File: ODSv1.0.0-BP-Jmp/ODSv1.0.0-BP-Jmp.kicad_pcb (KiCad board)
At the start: 2 copper layers, 150 x 150 mm, 73 parts, among them J1 Conn_01x16, J10 Conn_02x10_Odd_Even, J11 Conn_02x10_Odd_Even, J12 Conn_02x10_Odd_Even, J13 Conn_02x10_Odd_Even, J14 Conn_02x10_Odd_Even, J15 Conn_02x10_Odd_Even, J16 Conn_02x10_Odd_Even, J17 Conn_02x10_Odd_Even, J18 Conn_02x10_Odd_Even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

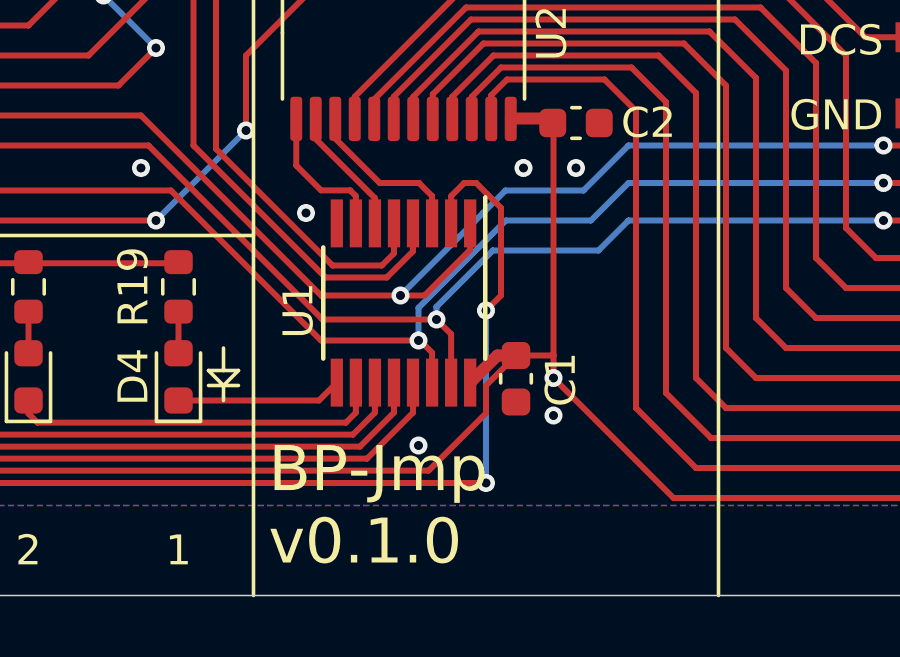
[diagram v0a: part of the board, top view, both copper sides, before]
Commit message: Disconnect BT & BP-Jmp backbone MAX7317 DOUT (#16); make DOUT output pin
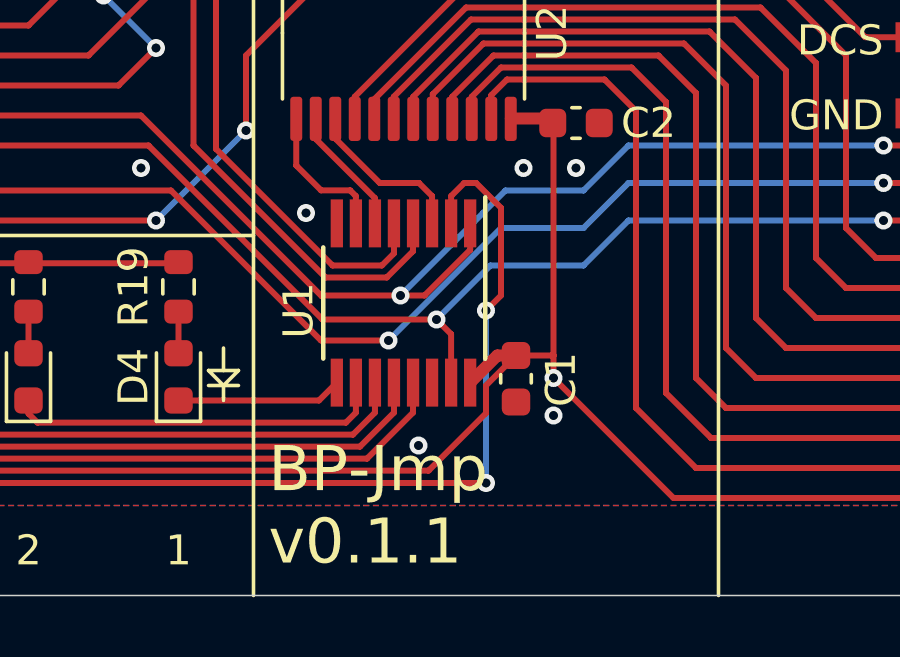
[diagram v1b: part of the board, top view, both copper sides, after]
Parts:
- D1, D2, D3: value Blue -> Green
- D4, D5, D6, D7, D8: value Yellow -> Blue
- R16: value 270 -> 7.5k
- R17: value 1k -> 7.5k
- R18: value 1.2k -> 20k
- R19, R20, R21, R22, R23: value 560 -> 2k
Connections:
- U1 pad 14: /SPI0_CIPO -> (no net)
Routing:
- net /SPI0_CIPO: track 265.8 -> 263.6 mm
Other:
- board text added: "BP-Jmp v0.1.1"
- board text removed: "BP-Jmp v0.1.0"

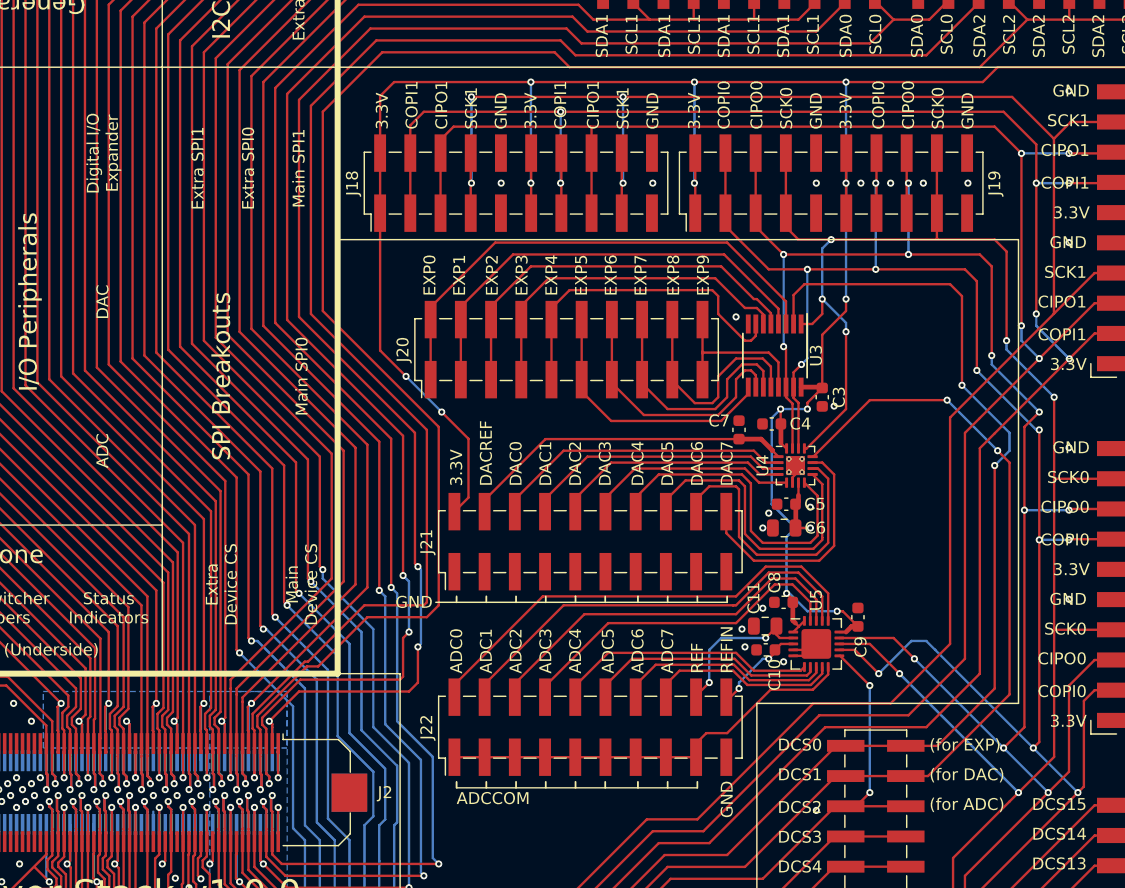
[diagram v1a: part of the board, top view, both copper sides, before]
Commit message: Replace DAC with a second MAX7317 expander with pullup resistors
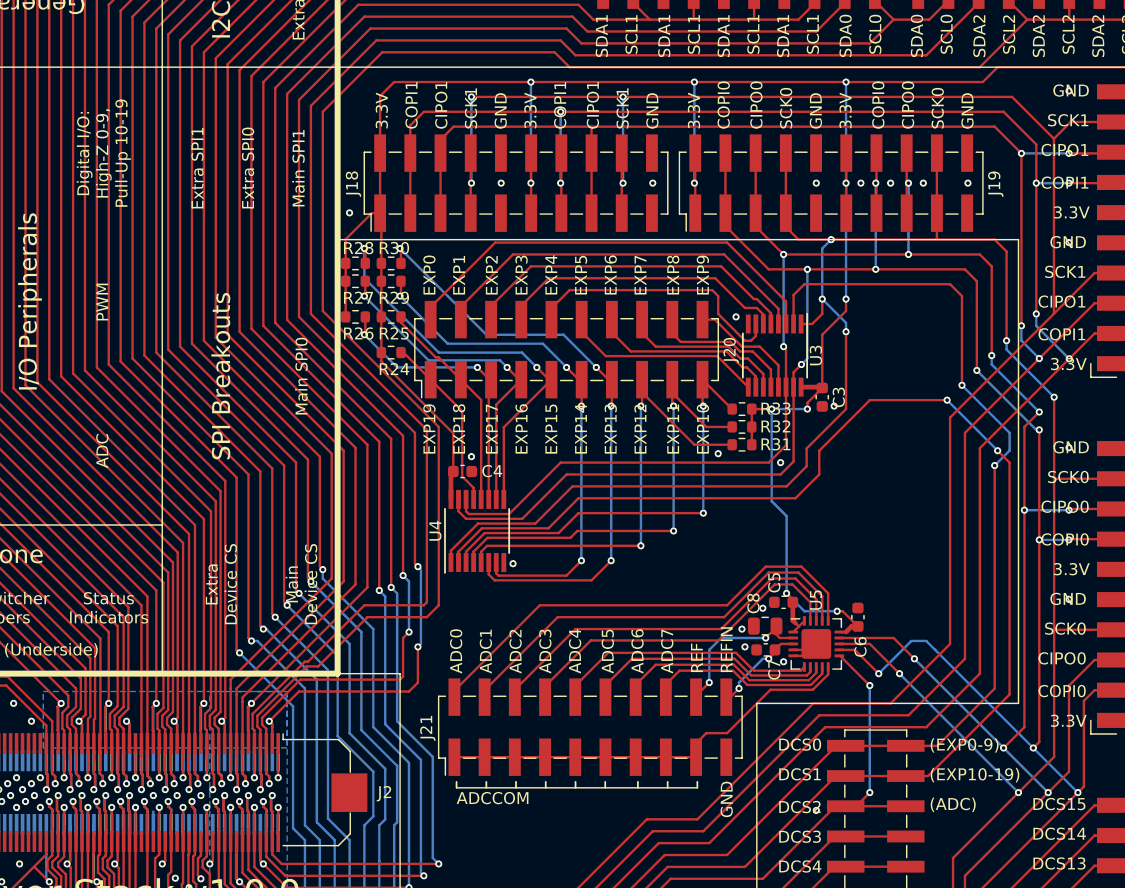
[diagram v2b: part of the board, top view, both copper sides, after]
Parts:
- removed the C5 at (142.5, 150.8)
- removed the C6 at (142.3, 152.8)
- removed the C7 at (138.5, 144.5)
- removed the J21 at (126.0, 153.9)
- added R24: 20k, Resistor_SMD:R_0603_1608Metric, F.Cu at (109.2, 138.0)
- added R25: 20k, Resistor_SMD:R_0603_1608Metric, F.Cu at (109.2, 135.0)
- added R26: 20k, Resistor_SMD:R_0603_1608Metric, F.Cu at (106.2, 135.0)
- added R27: 20k, Resistor_SMD:R_0603_1608Metric, F.Cu at (106.2, 132.0)
- added R28: 20k, Resistor_SMD:R_0603_1608Metric, F.Cu at (106.2, 130.5)
- added R29: 20k, Resistor_SMD:R_0603_1608Metric, F.Cu at (109.2, 132.0)
- added R30: 20k, Resistor_SMD:R_0603_1608Metric, F.Cu at (109.2, 130.5)
- added R31: 20k, Resistor_SMD:R_0603_1608Metric, F.Cu at (138.8, 145.8)
- added R32: 20k, Resistor_SMD:R_0603_1608Metric, F.Cu at (138.8, 144.2)
- added R33: 20k, Resistor_SMD:R_0603_1608Metric, F.Cu at (138.8, 142.8)
- C4: value 0.1uF -> 0.047uF
- U4: value DACx0508xRTE -> MAX7317; footprint Package_DFN_QFN:WQFN-16-1EP_3x3mm_P0.5mm_EP1.6x1.6mm_ThermalVias -> Package_SO:QSOP-16_3.9x4.9mm_P0.635mm
- moved U4 27.3 mm to (116.5, 153.0), turned to 90 degrees
- moved C4 26.3 mm to (115.2, 148.0), turned to 0 degrees
- renumbered C8 to C5, C9 to C6, C10 to C7, C11 to C8, J22 to J21
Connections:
- J20 pad 1: /IO Expander/EXPIO0 -> /IO Expander/EXPIO19
- J20 pad 11: /IO Expander/EXPIO5 -> /IO Expander/EXPIO14
- J20 pad 13: /IO Expander/EXPIO6 -> /IO Expander/EXPIO13
- J20 pad 15: /IO Expander/EXPIO7 -> /IO Expander/EXPIO12
- J20 pad 17: /IO Expander/EXPIO8 -> /IO Expander/EXPIO11
- J20 pad 19: /IO Expander/EXPIO9 -> /IO Expander/EXPIO10
- J20 pad 3: /IO Expander/EXPIO1 -> /IO Expander/EXPIO18
- J20 pad 5: /IO Expander/EXPIO2 -> /IO Expander/EXPIO17
- J20 pad 7: /IO Expander/EXPIO3 -> /IO Expander/EXPIO16
- J20 pad 9: /IO Expander/EXPIO4 -> /IO Expander/EXPIO15
- U4 pad 1: /IO Expander/DACREF -> /SPI0_SCK
- U4 pad 10: /IO Expander/DAC6 -> /IO Expander/EXPIO16
- U4 pad 11: /IO Expander/DAC7 -> /IO Expander/EXPIO17
- U4 pad 12: /~DCS1~ -> /IO Expander/EXPIO18
- U4 pad 13: /SPI0_SCK -> /IO Expander/EXPIO19
- U4 pad 14: /SPI0_COPI -> /SPI0_CIPO
- U4 pad 15: /SPI0_CIPO -> /SPI0_COPI
- U4 pad 2: /IO Expander/DAC0 -> /~DCS1~
- U4 pad 3: /IO Expander/DAC1 -> /IO Expander/EXPIO10
- U4 pad 4: /IO Expander/DAC2 -> /IO Expander/EXPIO11
- U4 pad 5: /IO Expander/DAC3 -> /IO Expander/EXPIO12
- U4 pad 6: GND -> /IO Expander/EXPIO13
- U4 pad 7: +3V3 -> /IO Expander/EXPIO14
- U4 pad 8: /IO Expander/DAC4 -> GND
- U4 pad 9: /IO Expander/DAC5 -> /IO Expander/EXPIO15
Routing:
- net /IO Expander/EXPIO13: track 0.00 -> 51.1 mm, vias 0 -> 4
- net /IO Expander/EXPIO14: track 0.00 -> 43.4 mm, vias 0 -> 4
- net /IO Expander/EXPIO12: track 0.00 -> 39.0 mm, vias 0 -> 2
- net /IO Expander/EXPIO11: track 0.00 -> 38.6 mm, vias 0 -> 2
- net /IO Expander/EXPIO10: track 0.00 -> 37.0 mm, vias 0 -> 2
- net /~DCS1~: track 83.7 -> 118.9 mm
- net /SPI0_SCK: track 253.6 -> 288.8 mm
- net /IO Expander/EXPIO15: track 0.00 -> 34.8 mm, vias 0 -> 2
- net /SPI0_COPI: track 265.3 -> 297.7 mm
- net /SPI0_CIPO: track 263.6 -> 293.5 mm
- net /IO Expander/DACREF: track 28.4 -> 0.00 mm
- net /IO Expander/EXPIO16: track 0.00 -> 28.3 mm, vias 0 -> 2
- net /IO Expander/DAC4: track 27.2 -> 0.00 mm
- net /IO Expander/DAC5: track 25.7 -> 0.00 mm
- net /IO Expander/DAC0: track 25.3 -> 0.00 mm
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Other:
- board text added: "(ADC)"
- board text added: "(EXP0-9)"
- board text added: "(EXP10-19)"
- board text added: "Digital I/O: High-Z 0-9, Pull-Up 10-19"
- board text added: "EXP10"
- board text added: "EXP11"
- board text added: "EXP12"
- board text added: "EXP13"
- board text added: "EXP14"
- board text added: "EXP15"
- board text added: "EXP16"
- board text added: "EXP17"
- board text added: "EXP18"
- board text added: "EXP19"
- board text added: "PWM"
- board text removed: "(for ADC)"
- board text removed: "(for DAC)"
- board text removed: "(for EXP)"
- board text removed: "DAC"
- board text removed: "DAC0"
- board text removed: "DAC1"
- board text removed: "DAC2"
- board text removed: "DAC3"
- board text removed: "DAC4"
- board text removed: "DAC5"
- board text removed: "DAC6"
- board text removed: "DAC7"
- board text removed: "DACREF"
- board text removed: "Digital I/O Expander"

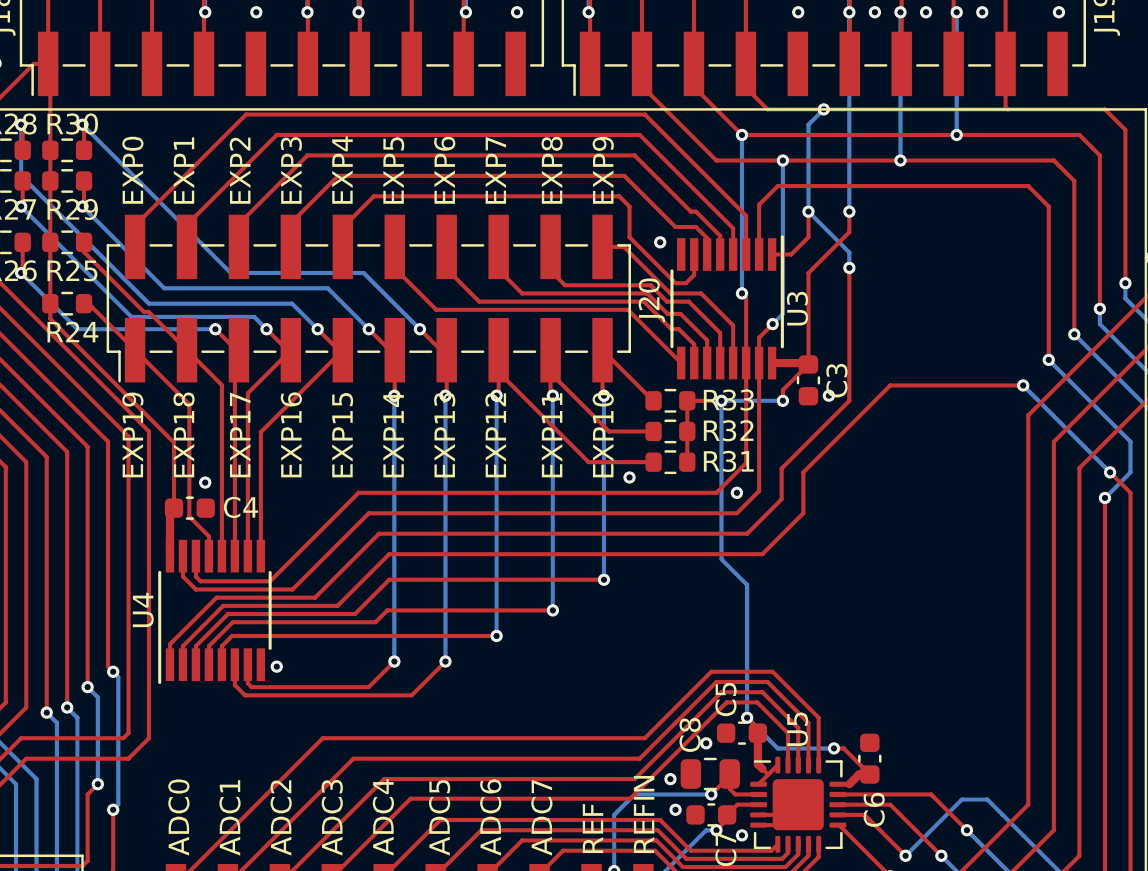
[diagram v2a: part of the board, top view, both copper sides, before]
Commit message: Insert 3-state buffers between MAX7317 DOUTs and CIPO in BP-Jmp (#16)
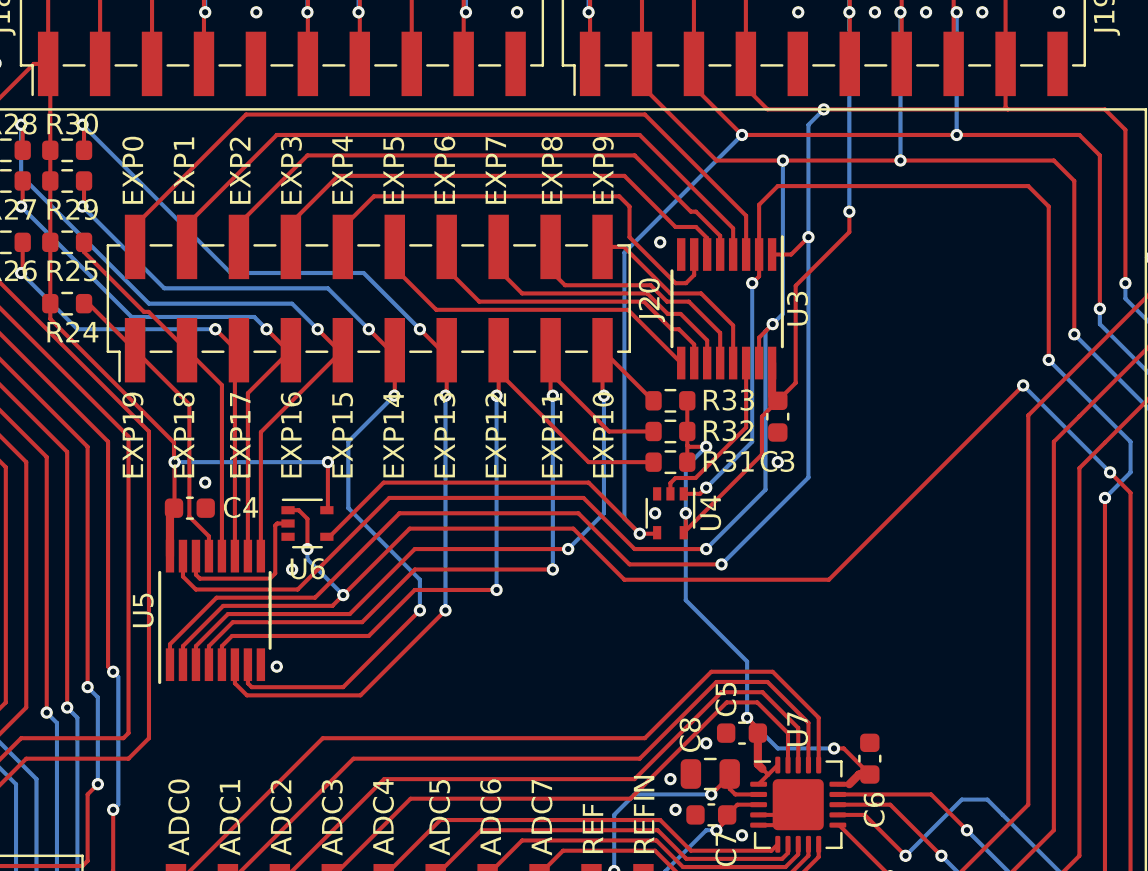
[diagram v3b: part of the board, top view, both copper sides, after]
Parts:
- added U4: NC7SZ125, Package_TO_SOT_SMD:SOT-353_SC-70-5, F.Cu at (138.8, 148.2)
- added U6: NC7SZ125, Package_TO_SOT_SMD:SOT-353_SC-70-5, F.Cu at (121.0, 148.8)
- moved C3 2.32 mm to (144.0, 143.5)
- renumbered U4 to U5, U5 to U7
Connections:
- U3 pad 14: /SPI0_CIPO -> Net-(U3-Pad14)
- U5 pad 14: /SPI0_CIPO -> Net-(U5-Pad14)
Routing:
- net +3V3: track 957.5 -> 972.4 mm, vias 25 -> 27
- net /~DCS0~: track 96.1 -> 109.8 mm, vias 2 -> 4
- net Net-(U3-Pad14): track 0.00 -> 8.50 mm
- net Net-(U5-Pad14): track 0.00 -> 7.98 mm
- net /~DCS1~: track 118.9 -> 125.4 mm, vias 2 -> 4
- net /SPI0_CIPO: track 293.5 -> 287.5 mm
- net /SPI0_COPI: track 297.7 -> 302.1 mm, vias 14 -> 15
- net /IO Expander/EXPIO14: track 43.4 -> 45.5 mm
- net /IO Expander/EXPIO10: track 37.0 -> 35.1 mm
- net /IO Expander/EXPIO13: track 51.1 -> 49.6 mm
- net /IO Expander/EXPIO12: track 39.0 -> 37.7 mm
- net /IO Expander/EXPIO11: track 38.6 -> 37.4 mm
- net /SPI0_SCK: track 288.8 -> 288.1 mm

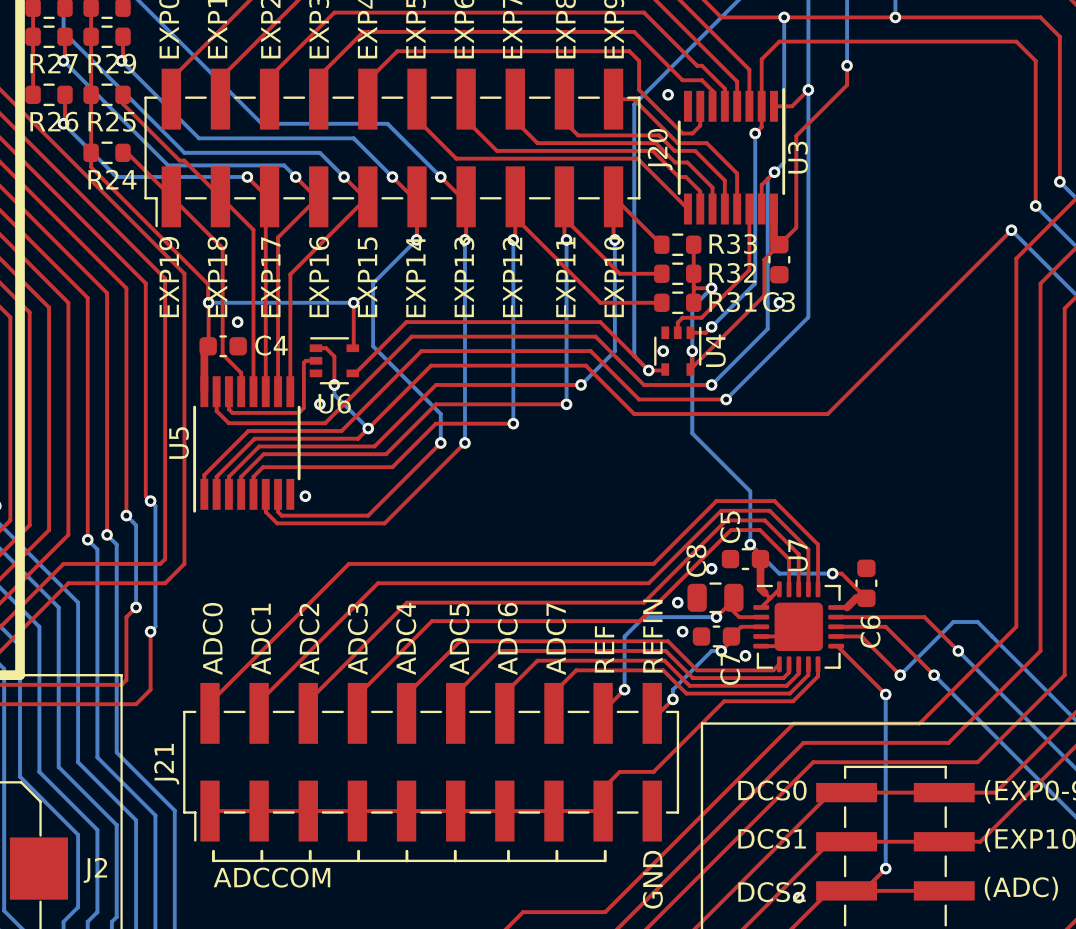
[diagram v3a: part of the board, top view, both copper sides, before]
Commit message: Consolidate free space by moving the AD7689 chip
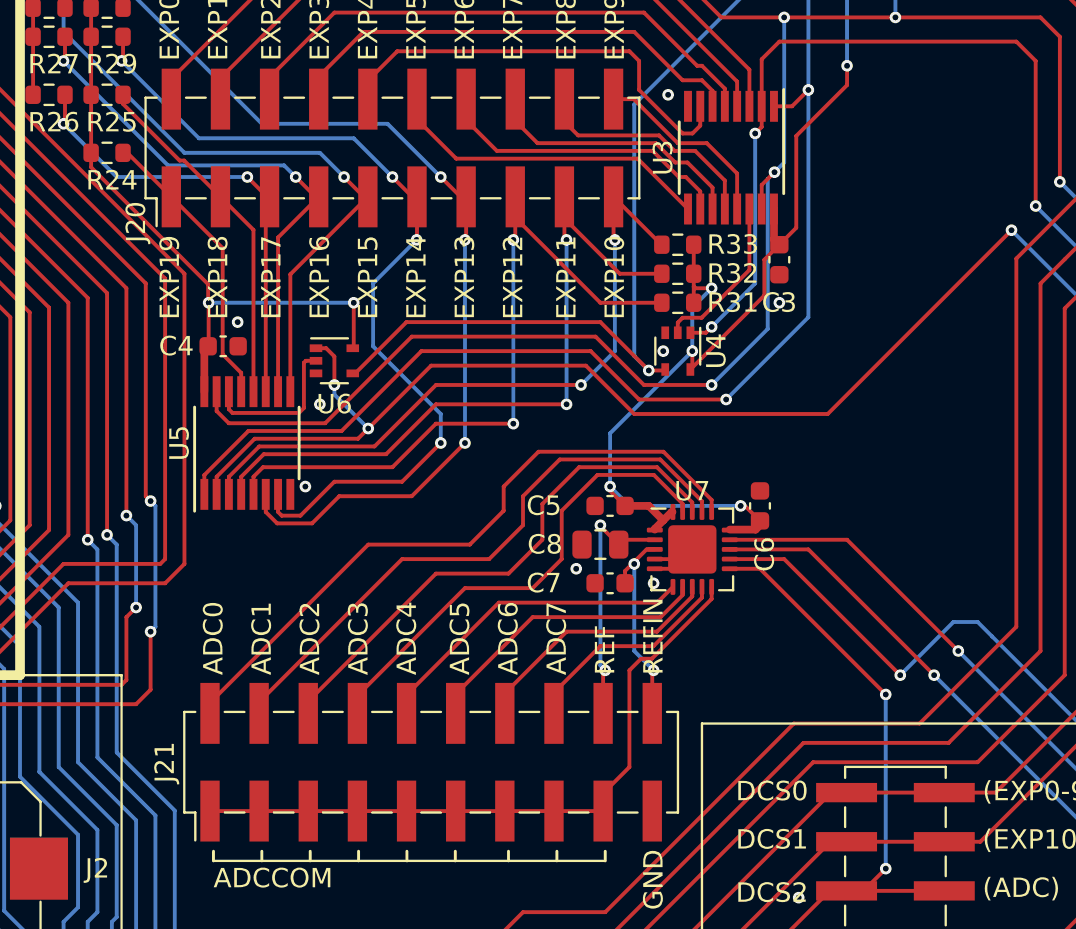
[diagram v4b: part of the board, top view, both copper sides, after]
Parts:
- moved C5 7.52 mm to (135.2, 156.2)
- moved C6 6.80 mm to (143.0, 156.2)
- moved U7 6.80 mm to (139.5, 158.5)
- moved C8 6.55 mm to (134.8, 158.2)
- moved C7 6.15 mm to (135.2, 160.2)
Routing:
- net /SPI0_COPI: track 302.1 -> 309.2 mm
- net /~DCS2~: track 45.0 -> 52.2 mm
- net /SPI0_SCK: track 288.1 -> 295.2 mm
- net /SPI0_CIPO: track 287.5 -> 294.6 mm
- net /IO Expander/ADC0: track 39.5 -> 34.2 mm
- net /IO Expander/ADC4: track 22.1 -> 17.0 mm
- net /IO Expander/ADC5: track 20.3 -> 15.3 mm
- net /IO Expander/ADC1: track 36.0 -> 31.0 mm
- net /IO Expander/ADC6: track 18.2 -> 13.3 mm
- net /IO Expander/ADC7: track 16.2 -> 11.3 mm
- net /IO Expander/ADC2: track 32.4 -> 27.8 mm
- net /IO Expander/ADC3: track 29.0 -> 25.0 mm
- net /IO Expander/REFIN: track 7.91 -> 10.8 mm
- net /IO Expander/ADCCOM: track 35.6 -> 34.6 mm
- net +3V3: track 972.4 -> 971.7 mm
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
